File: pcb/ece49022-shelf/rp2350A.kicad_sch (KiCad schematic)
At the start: 0 parts

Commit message: rp2350 inside
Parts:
- added C13, C17, C31: 10u, Capacitor_SMD:C_0805_2012Metric, symbol Device:C
- added C14, C15: 15p, Capacitor_SMD:C_0402_1005Metric, symbol Device:C
- added C16, C20, C23, C24, C25, C26, C27, C28, C29, C30: 100n, Capacitor_SMD:C_0402_1005Metric, symbol Device:C
- added C18, C19: 4.7u, RP2350_60QFN_minimal:C_0402_1005Metric_small_pads, symbol Device:C
- added C21, C22: 4.7u, Capacitor_SMD:C_0402_1005Metric, symbol Device:C
- added H1: MountingHole, MountingHole:MountingHole_2.7mm_M2.5, symbol Mechanical:MountingHole
- added J1: USB_B_Micro, 49022_Footprints:USB_Micro-B_Amphenol_10103594-0001LF_Horizontal_modified, symbol Connector:USB_B_Micro
- added J4: SM03B-SRSS-TB, Connector_JST:JST_SH_SM03B-SRSS-TB_1x03-1MP_P1.00mm_Horizontal, symbol Connector_Generic_MountingPin:Conn_01x03_MountingPin
- added L3: 3.3u, 49022_Footprints:L_pol_2016, symbol Device:L
- added R11, R13: DNF, Resistor_SMD:R_0402_1005Metric, symbol Device:R
- added R12: 0, Resistor_SMD:R_0402_1005Metric, symbol Device:R
- added R14, R15, R17: 1k, Resistor_SMD:R_0402_1005Metric, symbol Device:R
- added R16: 33, Resistor_SMD:R_0402_1005Metric, symbol Device:R
- added R18, R19: 27, Resistor_SMD:R_0402_1005Metric, symbol Device:R
- added SW1, SW2: SW_Push, Button_Switch_SMD:SW_Push_1P1T_NO_Vertical_Wuerth_434133025816, symbol Switch:SW_Push
- added U3: W25Q128JVS, Package_SO:SOIC-8_5.23x5.23mm_P1.27mm, symbol Memory_Flash:W25Q128JVS
- added U4: NCP1117-3.3_SOT223, Package_TO_SOT_SMD:SOT-223-3_TabPin2, symbol Regulator_Linear:NCP1117-3.3_SOT223
- added U5: RP2350_60QFN, 49022_Footprints:RP2350-QFN-60-1EP_7x7_P0.4mm_EP3.4x3.4mm_ThermalVias, symbol MCU_RaspberryPi_RP2350:RP2350_60QFN
- added Y1: ABM8-272-T3, Crystal:Crystal_SMD_3225-4Pin_3.2x2.5mm, symbol Device:Crystal_GND24
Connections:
- new net: R19.2, U5.51 (USB_DM)
- new net: R18.2, U5.52 (USB_DP)
- new net: C15.1, R14.2, Y1.3
- new net: R15.1, SW2.1
- new net +1V1: C19.1, C20.1, C22.1, C23.1, L3.1, U5.23 (DVDD), U5.39 (DVDD), U5.50 (VREG_FB), U5.6 (DVDD)
- new net +3V3: C16.1, C17.1, C18.1, C24.1, C25.1, C26.1, C27.1, C28.1, C29.1, C30.1, C31.1, R13.1, R16.1, U3.8 (VCC), U4.2 (VO), U5.1 (IOVDD), U5.11 (IOVDD), U5.20 (IOVDD), U5.30 (IOVDD), U5.38 (IOVDD), U5.44 (ADC_AVDD), U5.45 (IOVDD), U5.49 (VREG_VIN), U5.53 (USB_OTP_VDD), U5.54 (QSPI_IOVDD)
- new net FLASH_SS: R11.2, R12.2, R13.2, U3.1 (~{CS})
- new net GND: C13.2, C14.2, C15.2, C16.2, C17.2, C18.2, C19.2, C20.2, C21.2, C22.2, C23.2, C24.2, C25.2, C26.2, C27.2, C28.2, C29.2, C30.2, C31.2, J1.5 (GND), J1.6 (Shield), J4.2 (Pin_2), J4.MP (MountPin), R15.2, SW1.1, U3.4 (GND), U4.1 (GND), U5.47 (VREG_PGND), U5.61 (GND), Y1.2, Y1.4
- new net GPIO0: R11.1, U5.2 (GPIO0)
- new net GPIO1: U5.3 (GPIO1)
- new net GPIO10: U5.14 (GPIO10)
- new net GPIO11: U5.15 (GPIO11)
- new net GPIO12: U5.16 (GPIO12)
- new net GPIO13: U5.17 (GPIO13)
- new net GPIO16: U5.27 (GPIO16)
- new net GPIO17: U5.28 (GPIO17)
- new net GPIO18: U5.29 (GPIO18)
- new net GPIO19: U5.31 (GPIO19)
- new net GPIO2: U5.4 (GPIO2)
- new net GPIO20: U5.32 (GPIO20)
- new net GPIO21: U5.33 (GPIO21)
- new net GPIO22: U5.34 (GPIO22)
- new net GPIO23: U5.35 (GPIO23)
- new net GPIO24: U5.36 (GPIO24)
- new net GPIO25: U5.37 (GPIO25)
- new net GPIO26_ADC0: U5.40 (GPIO26_ADC0)
- new net GPIO27_ADC1: U5.41 (GPIO27_ADC1)
- new net GPIO28_ADC2: U5.42 (GPIO28_ADC2)
- new net GPIO29_ADC3: U5.43 (GPIO29_ADC3)
- new net GPIO3: U5.5 (GPIO3)
- new net GPIO4: U5.7 (GPIO4)
- new net GPIO5: U5.8 (GPIO5)
- new net GPIO6: U5.9 (GPIO6)
- new net GPIO7: U5.10 (GPIO7)
- new net GPIO8: U5.12 (GPIO8)
- new net GPIO9: U5.13 (GPIO9)
- new net I2C1_SCL: U5.19 (GPIO15)
- new net I2C1_SDA: U5.18 (GPIO14)
- new net QSPI_SCLK: U3.6 (CLK), U5.56 (QSPI_SCLK)
- new net QSPI_SD0: U3.5 (DI(IO0)), U5.57 (QSPI_SD0)
- new net QSPI_SD1: U3.2 (DO(IO1)), U5.59 (QSPI_SD1)
- new net QSPI_SD2: U3.3 (IO2), U5.58 (QSPI_SD2)
- new net QSPI_SD3: U3.7 (IO3), U5.55 (QSPI_SD3)
- new net QSPI_SS: R12.1, R17.1, U5.60 (QSPI_SS)
- new net RUN: SW2.2, U5.26 (RUN)
- new net SWCLK: J4.1 (Pin_1), U5.24 (SWCLK)
- new net SWD: J4.3 (Pin_3), U5.25 (SWD)
- new net USB_D+: J1.3 (D+), R18.1
- new net USB_D-: J1.2 (D-), R19.1
- new net VBUS: C13.1, J1.1 (VBUS), U4.3 (VI)
- new net VREG_AVDD: C21.1, R16.2, U5.46 (VREG_AVDD)
- new net VREG_LX: L3.2, U5.48 (VREG_LX)
- new net XIN: C14.1, U5.21 (XIN), Y1.1
- new net XOUT: R14.1, U5.22 (XOUT)
- new net ~{USB_BOOT}: R17.2, SW1.2
- no-connect marks 0 -> 1
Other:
- note added: "12MHz Crystal"
- note added: "Flash"
- note added: "IOs"
- note added: "JST Debug Connector"
- note added: "Make sure R7 and R8 are close to RP2350"
- note added: "Power"

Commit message: quicksave
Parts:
- removed R11: DNF, Resistor_SMD:R_0402_1005Metric, symbol Device:R
- added D1: D, symbol Device:D
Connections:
- net +3V3: now also D1.2 (A); no longer C16.1, C17.1, C18.1, C24.1, C25.1, C26.1, C27.1, C28.1, C29.1, C30.1, C31.1, R13.1, R16.1, U3.8 (VCC), U4.2 (VO), U5.1 (IOVDD), U5.11 (IOVDD), U5.20 (IOVDD), U5.30 (IOVDD), U5.38 (IOVDD), U5.44 (ADC_AVDD), U5.45 (IOVDD), U5.49 (VREG_VIN), U5.53 (USB_OTP_VDD), U5.54 (QSPI_IOVDD)
- net GPIO11 renamed I2C0_SDA
- net GPIO12 renamed I2C0_SCL
- new net +3V3_MCU: C16.1, C17.1, C18.1, C24.1, C25.1, C26.1, C27.1, C28.1, C29.1, C30.1, C31.1, D1.1 (K), R13.1, R16.1, U3.8 (VCC), U4.2 (VO), U5.1 (IOVDD), U5.11 (IOVDD), U5.20 (IOVDD), U5.30 (IOVDD), U5.38 (IOVDD), U5.44 (ADC_AVDD), U5.45 (IOVDD), U5.49 (VREG_VIN), U5.53 (USB_OTP_VDD), U5.54 (QSPI_IOVDD)
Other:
- note removed: "IOs"
- moved on the sheet: C14, C15, C16, C31, H1, J4, R12, R13, R14, R17, SW1, U3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

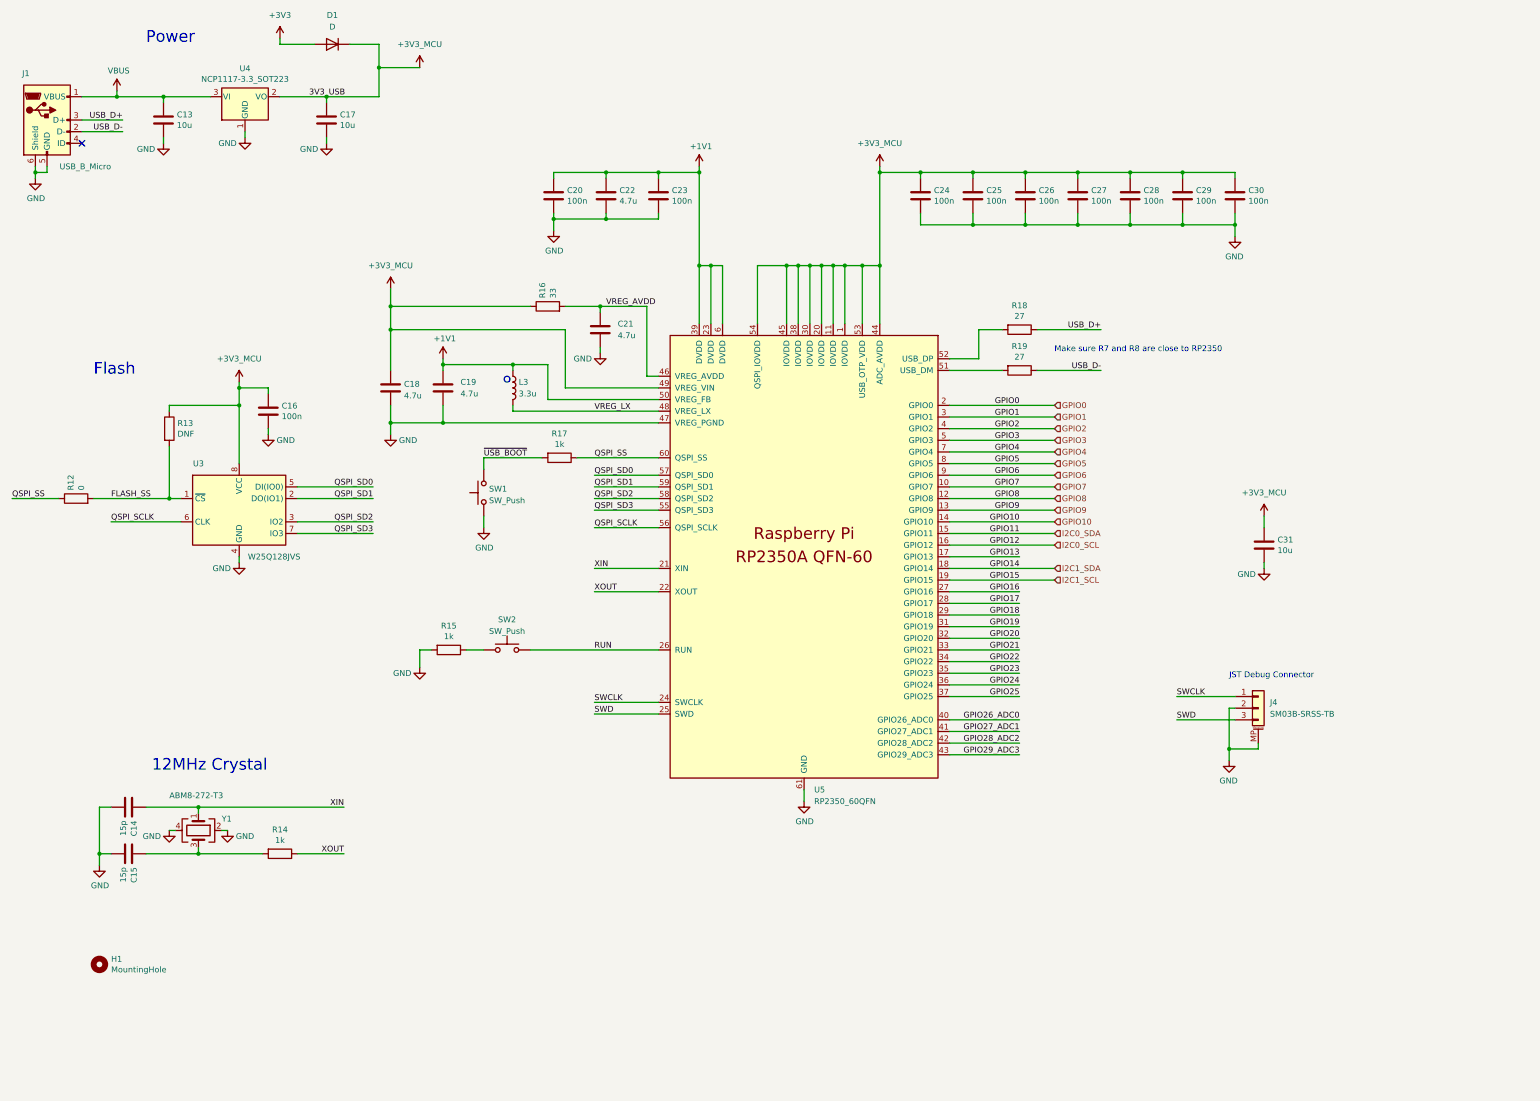
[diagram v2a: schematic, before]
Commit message: connecting top level
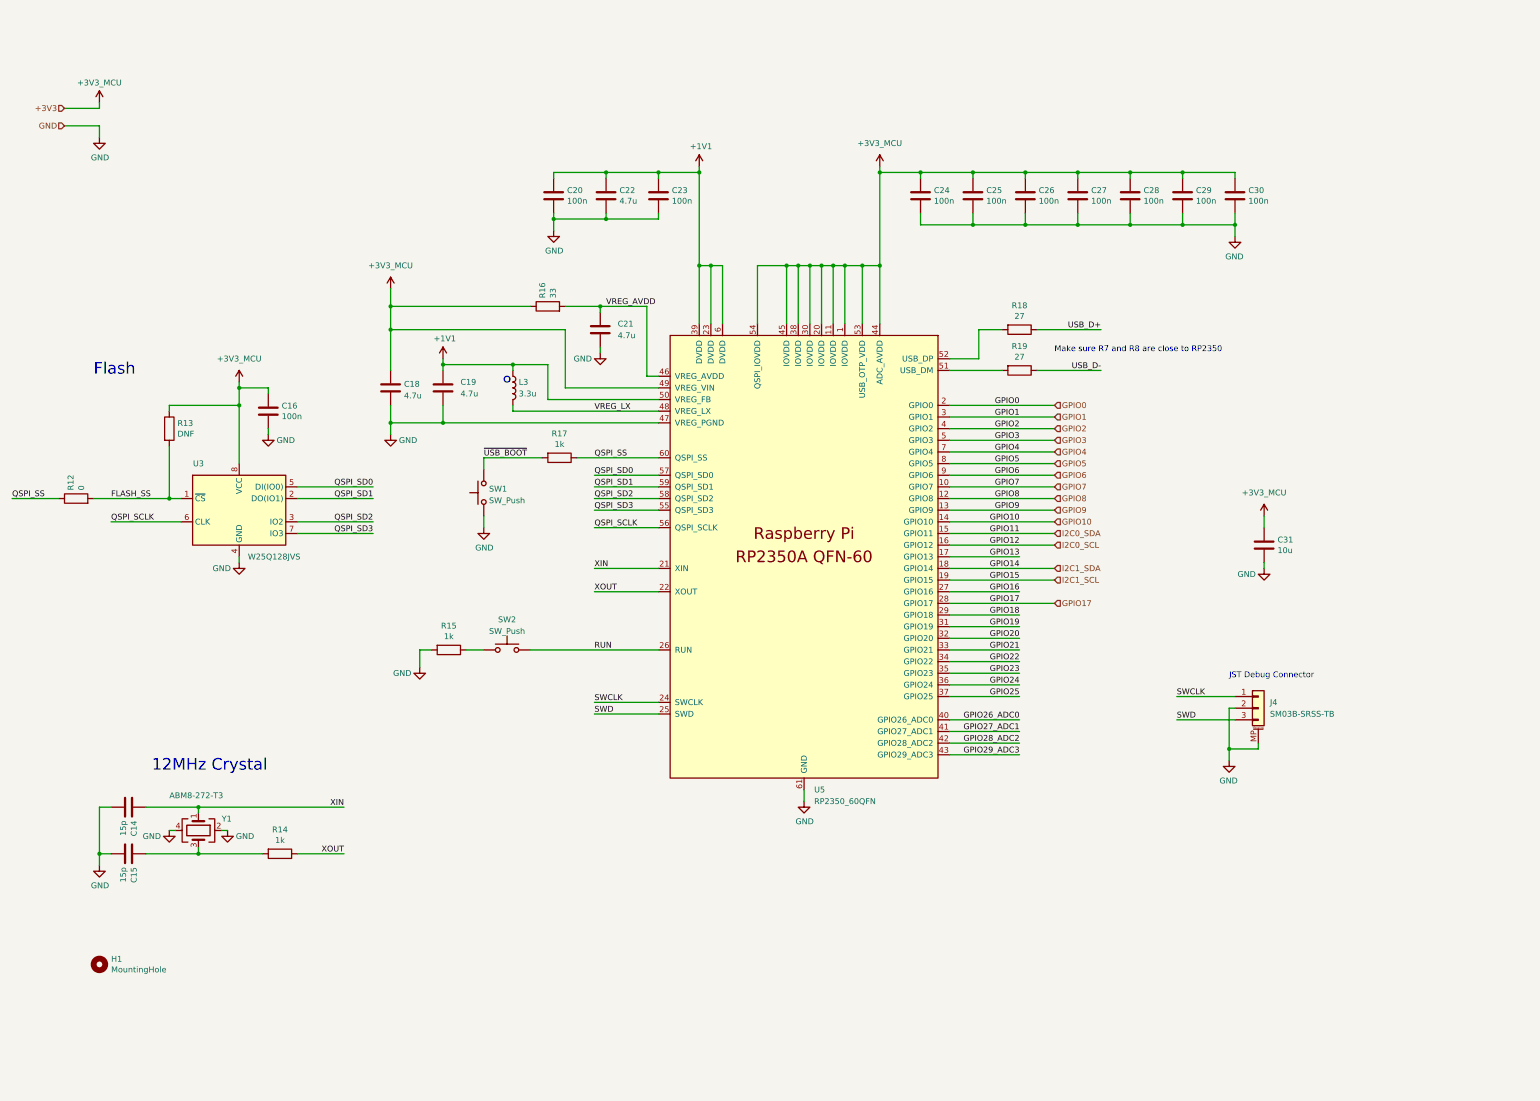
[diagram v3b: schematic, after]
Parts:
- removed C13, C17: 10u, Capacitor_SMD:C_0805_2012Metric, symbol Device:C
- removed D1: D, symbol Device:D
- removed J1: USB_B_Micro, 49022_Footprints:USB_Micro-B_Amphenol_10103594-0001LF_Horizontal_modified, symbol Connector:USB_B_Micro
- removed U4: NCP1117-3.3_SOT223, Package_TO_SOT_SMD:SOT-223-3_TabPin2, symbol Regulator_Linear:NCP1117-3.3_SOT223
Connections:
- no-connect marks 1 -> 0
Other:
- note removed: "Power"

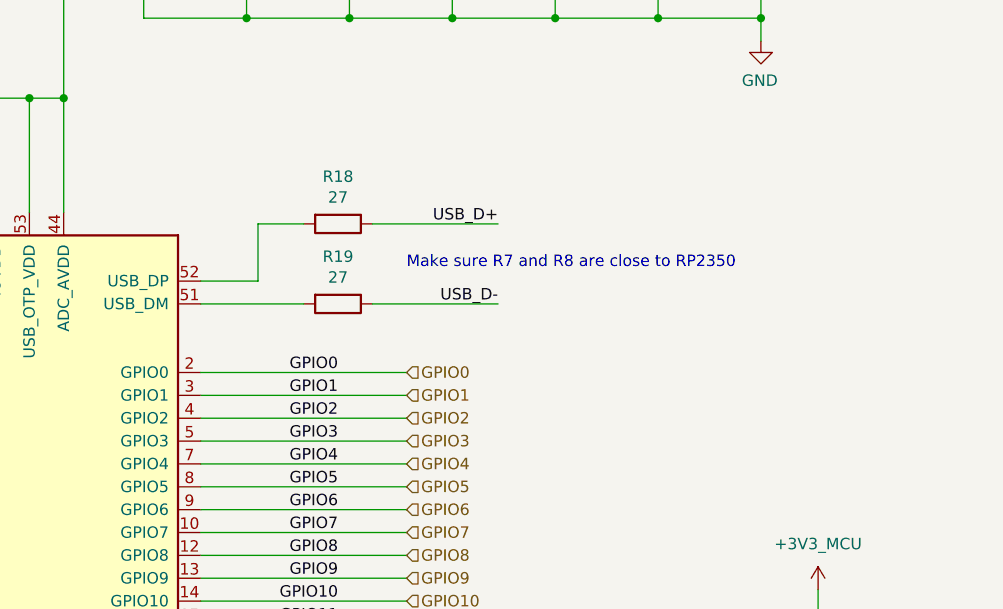
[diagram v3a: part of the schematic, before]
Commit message: Added components and got pcb layout imported
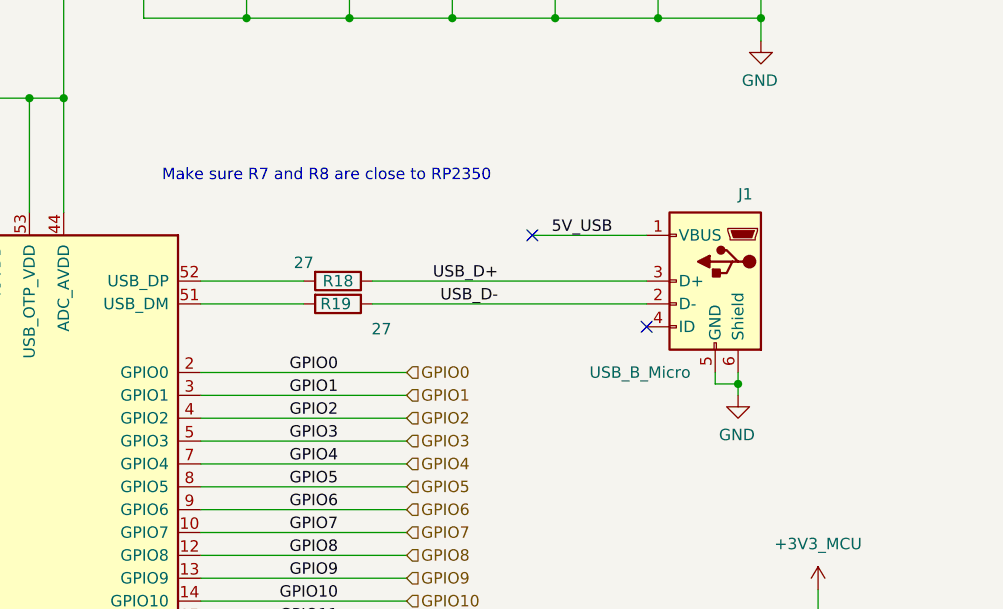
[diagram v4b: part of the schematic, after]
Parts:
- added J1: USB_B_Micro, 49022_Footprints:USB_Micro-B_Amphenol_10103594-0001LF_Horizontal_modified, symbol Connector:USB_B_Micro
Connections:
- net GND: now also J1.5 (GND), J1.6 (Shield)
- net USB_D+: now also J1.3 (D+)
- net USB_D-: now also J1.2 (D-)
- new net 5V_USB: J1.1 (VBUS)
- no-connect marks 0 -> 2
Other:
- moved on the sheet: R18
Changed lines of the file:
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@@
 	(text "Make sure R7 and R8 are close to RP2350\n"
 		(exclude_from_sim no)
-		(at 251.46 91.44 0)
+		(at 224.282 81.788 0)
 		(effects
 			(font
@@
 	)
 	(junction
+		(at 288.29 104.14)
+		(diameter 0)
+		(color 0 0 0 0)
+	)
+	(junction
 		(at 198.12 72.39)
 		(diameter 0)
@@
 		(color 0 0 0 0)
 	)
+	(no_connect
+		(at 265.43 87.63)
+	)
+	(no_connect
+		(at 278.13 97.79)
+	)
 	(wire
 		(pts
-			(xy 228.6 92.71) (xy 234.95 92.71)
+			(xy 228.6 92.71) (xy 240.03 92.71)
 		)
 		(stroke
@@
 	(wire
 		(pts
+			(xy 278.13 87.63) (xy 265.43 87.63)
+		)
+		(stroke
+			(width 0)
+			(type default)
+		)
+	)
+	(wire
+		(pts
+			(xy 288.29 102.87) (xy 288.29 104.14)
+		)
+		(stroke
+			(width 0)
+			(type default)
+		)
+	)
+	(wire
+		(pts
 			(xy 137.16 156.21) (xy 165.1 156.21)
 		)
@@
 	(wire
 		(pts
+			(xy 285.75 102.87) (xy 285.75 104.14)
+		)
+		(stroke
+			(width 0)
+			(type default)
+		)
+	)
+	(wire
+		(pts
+			(xy 288.29 104.14) (xy 288.29 105.41)
+		)
+		(stroke
+			(width 0)
+			(type default)
+		)
+	)
+	(wire
+		(pts
 			(xy 58.42 104.14) (xy 58.42 102.87)
 		)
@@
 	(wire
 		(pts
-			(xy 234.95 86.36) (xy 240.03 86.36)
-		)
-		(stroke
-			(width 0)
-			(type default)
-		)
-	)
-	(wire
-		(pts
 			(xy 213.36 52.07) (xy 222.25 52.07)
 		)
@@
 	(wire
 		(pts
-			(xy 234.95 86.36) (xy 234.95 92.71)
-		)
-		(stroke
-			(width 0)
-			(type default)
-		)
-	)
-	(wire
-		(pts
 			(xy 245.11 52.07) (xy 256.54 52.07)
 		)
@@
 	(wire
 		(pts
-			(xy 247.65 95.25) (xy 261.62 95.25)
+			(xy 247.65 95.25) (xy 278.13 95.25)
 		)
 		(stroke
@@
 	(wire
 		(pts
-			(xy 247.65 86.36) (xy 261.62 86.36)
+			(xy 247.65 92.71) (xy 278.13 92.71)
 		)
 		(stroke
@@
 	(wire
 		(pts
+			(xy 285.75 104.14) (xy 288.29 104.14)
+		)
+		(stroke
+			(width 0)
+			(type default)
+		)
+	)
+	(wire
+		(pts
 			(xy 118.11 93.98) (xy 133.35 93.98)
 		)
@@
 	)
 	(label "USB_D+"
-		(at 261.62 86.36 180)
+		(at 261.62 92.71 180)
 		(effects
 			(font
@@
 		)
 	)
+	(label "5V_USB"
+		(at 274.32 87.63 180)
+		(effects
+			(font
+				(size 1.27 1.27)
+			)
+			(justify right bottom)
+		)
+	)
 	(label "GPIO15"
 		(at 243.84 140.97 180)
@@
 	)
 	(symbol
+		(lib_id "Connector:USB_B_Micro")
+		(at 285.75 92.71 0)
+		(mirror y)
+		(unit 1)
+		(exclude_from_sim no)
+		(in_bom yes)
+		(on_board yes)
+		(dnp no)
+		(property "Reference" "J1"
+			(at 288.29 83.058 0)
+			(effects
+				(font
+					(size 1.27 1.27)
+				)
+				(justify right)
+			)
+		)
+		(property "Value" "USB_B_Micro"
+			(at 271.78 102.87 0)
+			(effects
+				(font
+					(size 1.27 1.27)
+				)
+				(justify right)
+			)
+		)
+		(property "Footprint" "49022_Footprints:USB_Micro-B_Amphenol_10103594-0001LF_Horizontal_modified"
+			(at 281.94 93.98 0)
+			(effects
+				(font
+					(size 1.27 1.27)
+				)
+				(hide yes)
+			)
+		)
+		(property "Datasheet" "~"
+			(at 281.94 93.98 0)
+			(effects
+				(font
+					(size 1.27 1.27)
+				)
+				(hide yes)
+			)
+		)
+		(property "Description" ""
+			(at 285.75 92.71 0)
+			(effects
+				(font
+					(size 1.27 1.27)
+				)
+			)
+		)
+		(pin "1"
+		)
+		(pin "2"
+		)
+		(pin "3"
+		)
+		(pin "4"
+		)
+		(pin "5"
+		)
+		(pin "6"
+		)
+		(instances
+			(project "ece49022-shelf"
+				(path "/cb6cb1b4-c151-4aa2-8cd7-5430288cfa02/d90a4203-0e8d-4fad-a588-f7d5681a1fb6"
+					(reference "J1")
+					(unit 1)
+				)
+			)
+		)
+	)
+	(symbol
 		(lib_id "power:GND")
 		(at 196.85 189.23 0)
@@
 		(dnp no)
 		(property "Reference" "R19"
-			(at 243.84 89.9922 90)
+			(at 243.586 95.25 90)
 			(effects
 				(font
@@
 		)
 		(property "Value" "27"
-			(at 243.84 92.3036 90)
+			(at 248.666 98.044 90)
 			(effects
 				(font
@@
 	(symbol
 		(lib_id "Device:R")
-		(at 243.84 86.36 270)
+		(at 243.84 92.71 270)
 		(unit 1)
 		(exclude_from_sim no)
@@
 		(dnp no)
 		(property "Reference" "R18"
-			(at 243.84 81.1022 90)
+			(at 243.84 92.71 90)
 			(effects
 				(font
@@
 		)
 		(property "Value" "27"
-			(at 243.84 83.4136 90)
+			(at 240.03 90.678 90)
 			(effects
 				(font
@@
 		)
 		(property "Footprint" "Resistor_SMD:R_0402_1005Metric"
-			(at 243.84 84.582 90)
+			(at 243.84 90.932 90)
 			(effects
 				(font
@@
 		)
 		(property "Datasheet" "~"
-			(at 243.84 86.36 0)
+			(at 243.84 92.71 0)
 			(effects
 				(font
@@
 		)
 		(property "Description" ""
-			(at 243.84 86.36 0)
+			(at 243.84 92.71 0)
 			(effects
 				(font
@@
 					(unit 1)
 				)
+			)
+		)
+	)
+	(symbol
+		(lib_id "power:GND")
+		(at 288.29 105.41 0)
+		(mirror y)
+		(unit 1)
+		(exclude_from_sim no)
+		(in_bom yes)
+		(on_board yes)
+		(dnp no)
+		(property "Reference" "#PWR014"
+			(at 288.29 111.76 0)
+			(effects
+				(font
+					(size 1.27 1.27)
+				)
+				(hide yes)
+			)
+		)
+		(property "Value" "GND"
+			(at 288.163 109.8042 0)
+			(effects
+				(font
+					(size 1.27 1.27)
+				)
+			)
+		)
+		(property "Footprint" ""
+			(at 288.29 105.41 0)
+			(effects
+				(font
+					(size 1.27 1.27)
+				)
+				(hide yes)
+			)
+		)
+		(property "Datasheet" ""
+			(at 288.29 105.41 0)
+			(effects
+				(font
+					(size 1.27 1.27)
+				)
+				(hide yes)
+			)
+		)
+		(property "Description" ""
+			(at 288.29 105.41 0)
+			(effects
+				(font
+					(size 1.27 1.27)
+				)
+			)
+		)
+		(pin "1"
+		)
+		(instances
+			(project "ece49022-shelf"
+				(path "/cb6cb1b4-c151-4aa2-8cd7-5430288cfa02/d90a4203-0e8d-4fad-a588-f7d5681a1fb6"
+					(reference "#PWR014")
+					(unit 1)
+				)

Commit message: updated footprints, pcb
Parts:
- C18, C19: footprint RP2350_60QFN_minimal:C_0402_1005Metric_small_pads -> Capacitor_SMD:C_0402_1005Metric
- U3: footprint Package_SO:SOIC-8_5.23x5.23mm_P1.27mm -> Package_SO:SOIC-8_5.3x5.3mm_P1.27mm
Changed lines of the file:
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@@
 			)
 		)
-		(property "Footprint" "Package_SO:SOIC-8_5.23x5.23mm_P1.27mm"
+		(property "Footprint" "Package_SO:SOIC-8_5.3x5.3mm_P1.27mm"
 			(at 73.66 125.73 0)
 			(effects
@@
 			)
 		)
-		(property "Footprint" "RP2350_60QFN_minimal:C_0402_1005Metric_small_pads"
+		(property "Footprint" "Capacitor_SMD:C_0402_1005Metric"
 			(at 119.0752 102.87 0)
 			(effects
@@
 			)
 		)
-		(property "Footprint" "RP2350_60QFN_minimal:C_0402_1005Metric_small_pads"
+		(property "Footprint" "Capacitor_SMD:C_0402_1005Metric"
 			(at 107.6452 102.87 0)
 			(effects
